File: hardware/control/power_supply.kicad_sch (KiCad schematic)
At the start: 10 parts, among them U501 AMS1117-3.3, U502 AMS1117-5, U503 K78L15-1000R3

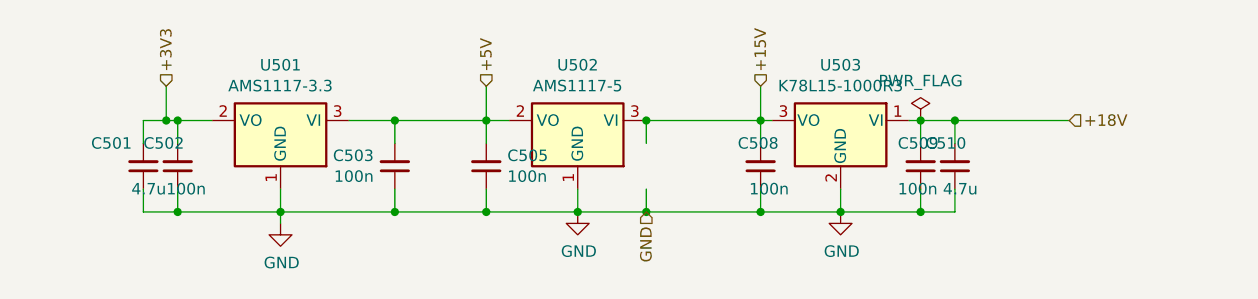
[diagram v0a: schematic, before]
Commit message: Organize schematics per domain
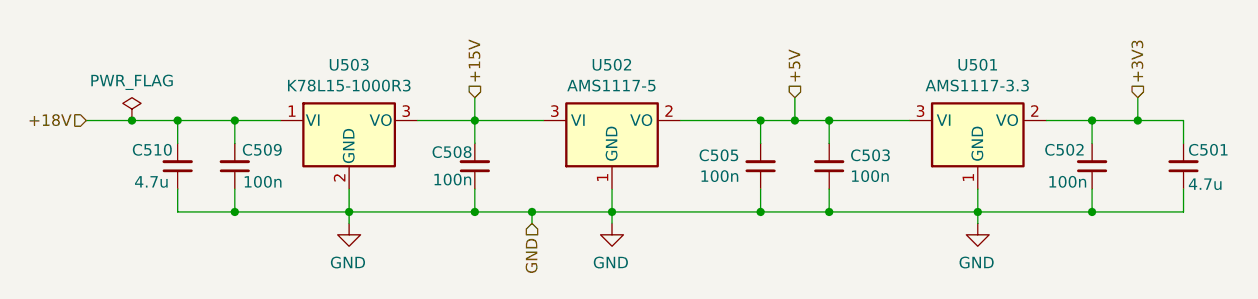
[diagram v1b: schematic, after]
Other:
- company: (none) -> Zenite Solar
- title: (none) -> Power Supplies
- moved on the sheet: C501, C502, C503, C505, C508, C509, C510, U501, U502, U503
